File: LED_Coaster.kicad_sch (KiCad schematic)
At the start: 2 parts

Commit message: Added outer ring of LEDs
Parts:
- removed D?: (no value), symbol LED:WS2812B
- added D1, D10, D11, D12, D13, D14, D15, D16, D17, D18, D19, D2, D20, D3, D4, D5, D6, D7, D8, D9: WS2812B, LED_SMD:LED_WS2812B_PLCC4_5.0x5.0mm_P3.2mm, symbol LED:WS2812B
- U1: renamed from U?; value (none) -> ATmega32U4-A; footprint (none) -> Package_QFP:TQFP-44_10x10mm_P0.8mm
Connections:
- new net: D7.2 (DOUT), D8.4 (DIN)
- new net: D6.2 (DOUT), D7.4 (DIN)
- new net: D17.2 (DOUT), D18.4 (DIN)
- new net: D16.2 (DOUT), D17.4 (DIN)
- new net: D14.2 (DOUT), D15.4 (DIN)
- new net: D13.2 (DOUT), D14.4 (DIN)
- new net: D10.4 (DIN), D9.2 (DOUT)
- new net: D8.2 (DOUT), D9.4 (DIN)
- new net: D18.2 (DOUT), D19.4 (DIN)
- new net: D15.2 (DOUT), D16.4 (DIN)
- new net: D10.2 (DOUT), D11.4 (DIN)
- new net: D1.2 (DOUT), D2.4 (DIN)
- new net: D12.2 (DOUT), D13.4 (DIN)
- new net: D5.2 (DOUT), D6.4 (DIN)
- new net: D11.2 (DOUT), D12.4 (DIN)
- new net: D4.2 (DOUT), D5.4 (DIN)
- new net: D2.2 (DOUT), D3.4 (DIN)
- new net: D19.2 (DOUT), D20.4 (DIN)
- new net: D3.2 (DOUT), D4.4 (DIN)
- new net +5V: D1.1 (VDD), D10.1 (VDD), D11.1 (VDD), D12.1 (VDD), D13.1 (VDD), D14.1 (VDD), D15.1 (VDD), D16.1 (VDD), D17.1 (VDD), D18.1 (VDD), D19.1 (VDD), D2.1 (VDD), D20.1 (VDD), D3.1 (VDD), D4.1 (VDD), D5.1 (VDD), D6.1 (VDD), D7.1 (VDD), D8.1 (VDD), D9.1 (VDD)
- new net GND: D1.3 (VSS), D10.3 (VSS), D11.3 (VSS), D12.3 (VSS), D13.3 (VSS), D14.3 (VSS), D15.3 (VSS), D16.3 (VSS), D17.3 (VSS), D18.3 (VSS), D19.3 (VSS), D2.3 (VSS), D20.3 (VSS), D3.3 (VSS), D4.3 (VSS), D5.3 (VSS), D6.3 (VSS), D7.3 (VSS), D8.3 (VSS), D9.3 (VSS)
- new net large_ring: D1.4 (DIN)
- no-connect marks 0 -> 1
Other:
- moved on the sheet: U1

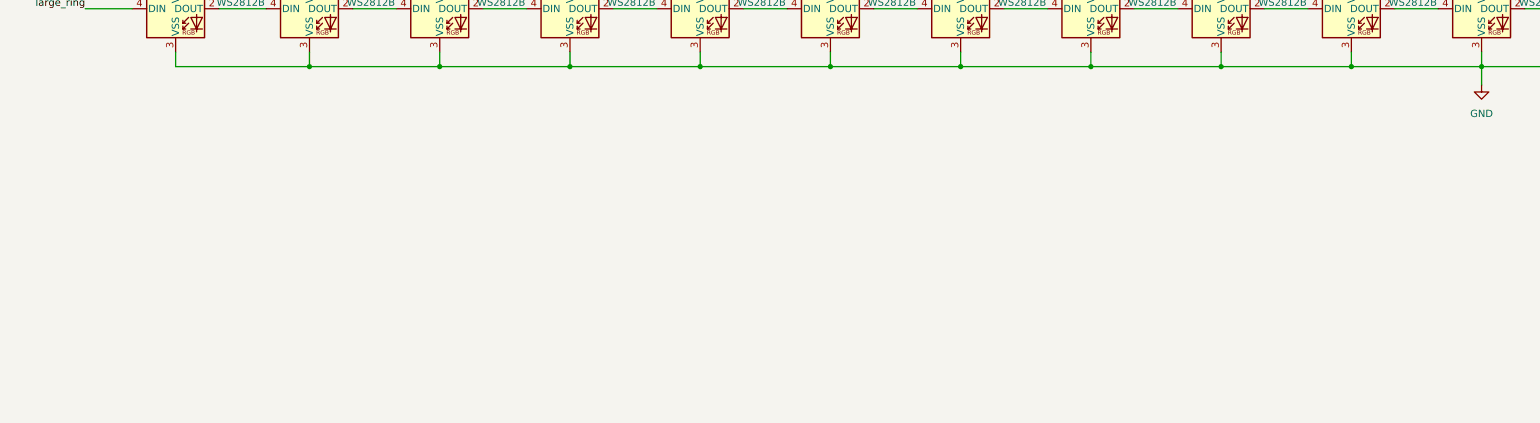
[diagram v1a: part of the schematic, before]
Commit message: Added inner ring of LEDs
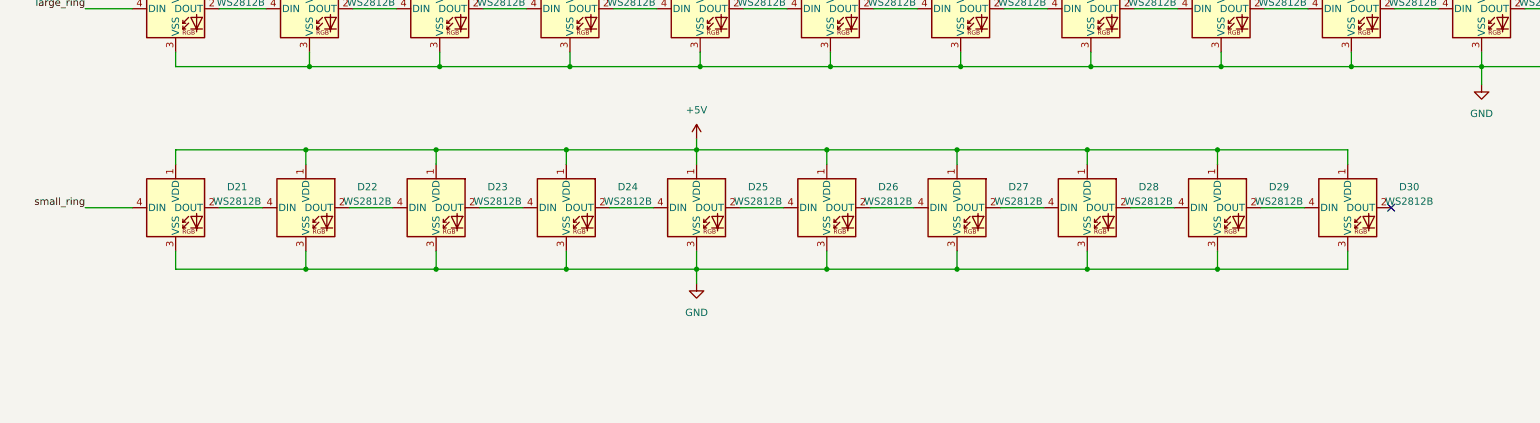
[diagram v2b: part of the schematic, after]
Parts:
- added D21, D22, D23, D24, D25, D26, D27, D28, D29, D30: WS2812B, LED_SMD:LED_WS2812B_PLCC4_5.0x5.0mm_P3.2mm, symbol LED:WS2812B
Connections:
- net +5V: now also D21.1 (VDD), D22.1 (VDD), D23.1 (VDD), D24.1 (VDD), D25.1 (VDD), D26.1 (VDD), D27.1 (VDD), D28.1 (VDD), D29.1 (VDD), D30.1 (VDD)
- net GND: now also D21.3 (VSS), D22.3 (VSS), D23.3 (VSS), D24.3 (VSS), D25.3 (VSS), D26.3 (VSS), D27.3 (VSS), D28.3 (VSS), D29.3 (VSS), D30.3 (VSS)
- new net: D29.2 (DOUT), D30.4 (DIN)
- new net: D21.2 (DOUT), D22.4 (DIN)
- new net: D28.2 (DOUT), D29.4 (DIN)
- new net: D27.2 (DOUT), D28.4 (DIN)
- new net: D26.2 (DOUT), D27.4 (DIN)
- new net: D24.2 (DOUT), D25.4 (DIN)
- new net: D23.2 (DOUT), D24.4 (DIN)
- new net: D25.2 (DOUT), D26.4 (DIN)
- new net: D22.2 (DOUT), D23.4 (DIN)
- new net small_ring: D21.4 (DIN)
- no-connect marks 1 -> 2

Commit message: MCU schematic halfway done
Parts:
- added C1: 1uF, Capacitor_SMD:C_0805_2012Metric_Pad1.18x1.45mm_HandSolder, symbol Device:C
- added C2: 10uF, Capacitor_SMD:C_0805_2012Metric_Pad1.18x1.45mm_HandSolder, symbol Device:C
- added C3, C4, C5: 0.1uF, Capacitor_SMD:C_0805_2012Metric_Pad1.18x1.45mm_HandSolder, symbol Device:C
- added C6, C7: 22pF, Capacitor_SMD:C_0805_2012Metric_Pad1.18x1.45mm_HandSolder, symbol Device:C
- added J1: USB_C_Receptacle_USB2.0, Connector_USB:USB_C_Receptacle_HRO_TYPE-C-31-M-12, symbol Connector:USB_C_Receptacle_USB2.0
- added R1, R4, R5, R6: 10K, Resistor_SMD:R_0805_2012Metric_Pad1.20x1.40mm_HandSolder, symbol Device:R
- added R2, R3: 22, Resistor_SMD:R_0805_2012Metric_Pad1.20x1.40mm_HandSolder, symbol Device:R
- added SW1: SW_Push, Button_Switch_SMD:SW_SPST_SKQG_WithoutStem, symbol Switch:SW_Push
- added Y1: Crystal_GND24, Crystal:Crystal_SMD_3225-4Pin_3.2x2.5mm_HandSoldering, symbol Device:Crystal_GND24
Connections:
- net +5V: now also U1.14 (VCC), U1.2 (UVCC), U1.24 (AVCC), U1.34 (VCC), U1.44 (AVCC), U1.7 (VBUS), C2.1, C3.1, C4.1, C5.1, R4.2
- net GND: now also U1.15 (GND), U1.23 (GND), U1.35 (GND), U1.43 (GND), U1.5 (UGND), C1.2, C2.2, C3.2, C4.2, C5.2, C6.1, C7.1, R1.2, SW1.1, Y1.2, Y1.4
- net at U1.13 (~{RESET}): now also R4.1, SW1.2
- net at U1.16 (XTAL2): now also C7.2, Y1.3
- net at U1.17 (XTAL1): now also C6.2, Y1.1
- net at U1.3 (D-): now also R3.2
- net at U1.33 (~{HWB}/PE2): now also R1.1
- net at U1.4 (D+): now also R2.2
- net at U1.6 (UCAP): now also C1.1
- new net: J1.A5 (CC1), R5.2
- new net: J1.B5 (CC2), R6.2
- new net: J1.A1 (GND), J1.A12 (GND), J1.B1 (GND), J1.B12 (GND)
- new net: J1.A4 (VBUS), J1.A9 (VBUS), J1.B4 (VBUS), J1.B9 (VBUS)
- new net D+: J1.A6 (D+), J1.B6 (D+), R2.1
- new net D-: J1.A7 (D-), J1.B7 (D-), R3.1
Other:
- moved on the sheet: U1

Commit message: Placed all components
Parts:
- added H1, H2, H3, H4: MountingHole, MountingHole:MountingHole_4.3mm_M4_Pad_Via, symbol Mechanical:MountingHole
- added SW2, SW3: SW_DIP_x01, Button_Switch_SMD:SW_SPDT_PCM12, symbol Switch:SW_DIP_x01
- R5, R6: value 10K -> 5.1K
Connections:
- net +5V: now also J1.A4 (VBUS), J1.A9 (VBUS), J1.B4 (VBUS), J1.B9 (VBUS), SW2.2, SW3.2; no longer D1.1 (VDD), D10.1 (VDD), D11.1 (VDD), D12.1 (VDD), D13.1 (VDD), D14.1 (VDD), D15.1 (VDD), D16.1 (VDD), D17.1 (VDD), D18.1 (VDD), D19.1 (VDD), D2.1 (VDD), D20.1 (VDD), D21.1 (VDD), D22.1 (VDD), D23.1 (VDD), D24.1 (VDD), D25.1 (VDD), D26.1 (VDD), D27.1 (VDD), D28.1 (VDD), D29.1 (VDD), D3.1 (VDD), D30.1 (VDD), D4.1 (VDD), D5.1 (VDD), D6.1 (VDD), D7.1 (VDD), D8.1 (VDD), D9.1 (VDD)
- net GND: now also J1.A1 (GND), J1.A12 (GND), J1.B1 (GND), J1.B12 (GND), J1.S1 (SHIELD), R5.1, R6.1
- new net: D21.1 (VDD), D22.1 (VDD), D23.1 (VDD), D24.1 (VDD), D25.1 (VDD), D26.1 (VDD), D27.1 (VDD), D28.1 (VDD), D29.1 (VDD), D30.1 (VDD), SW3.1
- new net: D1.1 (VDD), D10.1 (VDD), D11.1 (VDD), D12.1 (VDD), D13.1 (VDD), D14.1 (VDD), D15.1 (VDD), D16.1 (VDD), D17.1 (VDD), D18.1 (VDD), D19.1 (VDD), D2.1 (VDD), D20.1 (VDD), D3.1 (VDD), D4.1 (VDD), D5.1 (VDD), D6.1 (VDD), D7.1 (VDD), D8.1 (VDD), D9.1 (VDD), SW2.1
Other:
- moved on the sheet: C1, C2, C3, C4, C5, C6, C7, D1, D10, D11, D12, D13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

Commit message: Added a fuse
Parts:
- added D31, D32, D33: LED, LED_SMD:LED_0805_2012Metric_Pad1.15x1.40mm_HandSolder, symbol Device:LED
- added F1: Polyfuse, Fuse:Fuse_1206_3216Metric_Pad1.42x1.75mm_HandSolder, symbol Device:Polyfuse
- added R7, R8, R9: 150, Resistor_SMD:R_0805_2012Metric_Pad1.20x1.40mm_HandSolder, symbol Device:R
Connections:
- net +5V: now also F1.1; no longer J1.A4 (VBUS), J1.A9 (VBUS), J1.B4 (VBUS), J1.B9 (VBUS)
- net GND: now also D31.1 (K), D32.1 (K), D33.1 (K)
- net large_ring: now also U1.10 (PB2)
- net small_ring: now also U1.9 (PB1)
- net at D21.1 (VDD), D22.1 (VDD), D23.1 (VDD)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: now also R8.2
- net at D1.1 (VDD), D10.1 (VDD), D11.1 (VDD)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: now also R7.2
- net at U1.8 (PB0): now also R9.1
- new net: D31.2 (A), R7.1
- new net: F1.2, J1.A4 (VBUS), J1.A9 (VBUS), J1.B4 (VBUS), J1.B9 (VBUS)
- new net: D32.2 (A), R8.1
- new net: D33.2 (A), R9.2
- no-connect marks 2 -> 27
